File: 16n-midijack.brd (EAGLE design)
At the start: 248.9 x 120.7 mm, 108 parts, among them J1 PJ302M, J10 PJ302M, J11 PJ302M, J12 PJ302M, J13 PJ302M, J14 PJ302M, J15 PJ302M, J16 PJ302M, J2 PJ302M, J3 PJ302M, J4 PJ302M, J5 PJ302M, J6 PJ302M, J7 PJ302M, J8 PJ302M, J9 PJ302M, U1 MCP6004_SMD, U2 MCP6004_SMD, U3 MCP6004_SMD, U4 MCP6004_SMD, U5 MCP6004_SMD, U6 MCP6004_SMD, U7 MCP6004_SMD, U8 MCP6004_SMD

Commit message: Correcting outputs.
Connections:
- removed net N$11: R17.1, U3.8, U3.9
- removed net N$14: R22.1, U4.8, U4.9
- removed net N$17: R27.1, U5.8, U5.9
- removed net N$20: R32.1, U6.8, U6.9
- removed net N$23: R37.1, U7.8, U7.9
- removed net N$256: R12.1, U1.13, U1.14
- removed net N$257: R45.1, U2.13, U2.14
- removed net N$258: R47.1, U3.13, U3.14
- removed net N$259: R46.1, U4.13, U4.14
- removed net N$26: R42.1, U8.8, U8.9
- removed net N$260: R48.1, U5.13, U5.14
- removed net N$261: R49.1, U6.13, U6.14
- removed net N$262: R50.1, U7.13, U7.14
- removed net N$263: R51.1, U8.13, U8.14
- removed net N$5: R52.1, U2.8, U2.9
- removed net N$8: R7.1, U1.8, U1.9
- net A0: now also R7.1, U1.8, U1.9
- net A1: now also R12.1, U1.13, U1.14
- net A10: now also R32.1, U6.8, U6.9
- net A11: now also R49.1, U6.13, U6.14
- net A12: now also R37.1, U7.8, U7.9
- net A13: now also R50.1, U7.13, U7.14
- net A14: now also R42.1, U8.8, U8.9
- net A15: now also R51.1, U8.13, U8.14
- net A2: now also R52.1, U2.8, U2.9
- net A3: now also R45.1, U2.13, U2.14
- net A4: now also R17.1, U3.8, U3.9
- net A5: now also R47.1, U3.13, U3.14
- net A6: now also R22.1, U4.8, U4.9
- net A7: now also R46.1, U4.13, U4.14
- net A8: now also R27.1, U5.8, U5.9
- net A9: now also R48.1, U5.13, U5.14
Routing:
- net N$8: track 140.4 -> 0.00 mm
- net A0: track 32.3 -> 169.5 mm
- net N$5: track 123.3 -> 0.00 mm
- net A2: track 64.1 -> 183.2 mm
- net N$256: track 117.9 -> 0.00 mm
- net N$11: track 116.9 -> 0.00 mm
- net A4: track 91.8 -> 205.8 mm
- net N$263: track 110.8 -> 0.00 mm
- net N$257: track 108.8 -> 0.00 mm
- net N$14: track 107.4 -> 0.00 mm
- net A6: track 120.5 -> 225.1 mm
- net N$17: track 102.5 -> 0.00 mm
- net N$26: track 101.8 -> 0.00 mm, vias 2 -> 0
- net N$258: track 100.3 -> 0.00 mm
- net A14: track 204.6 -> 303.3 mm, vias 2 -> 4
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
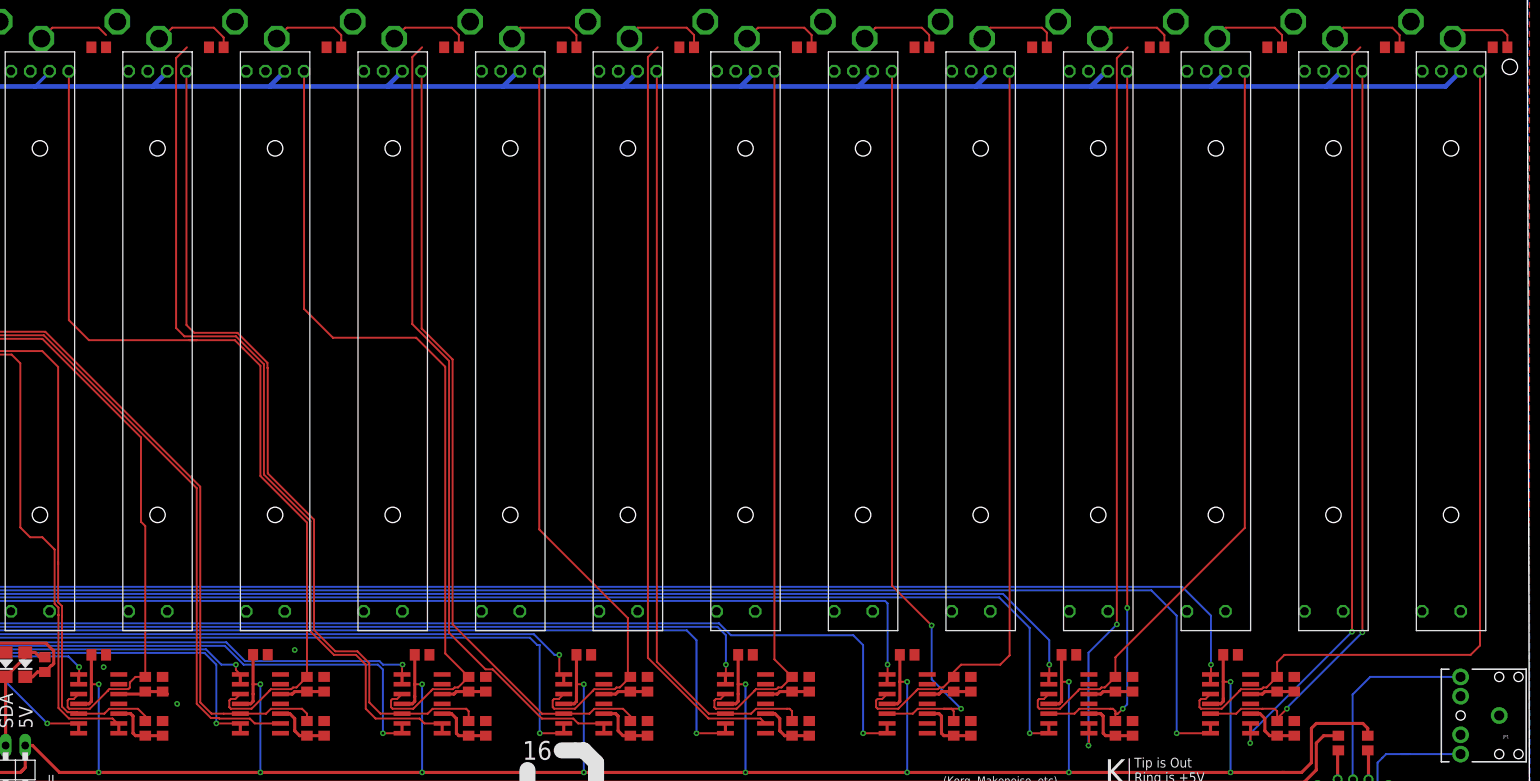
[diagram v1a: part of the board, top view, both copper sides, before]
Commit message: Remove legacy trace names.
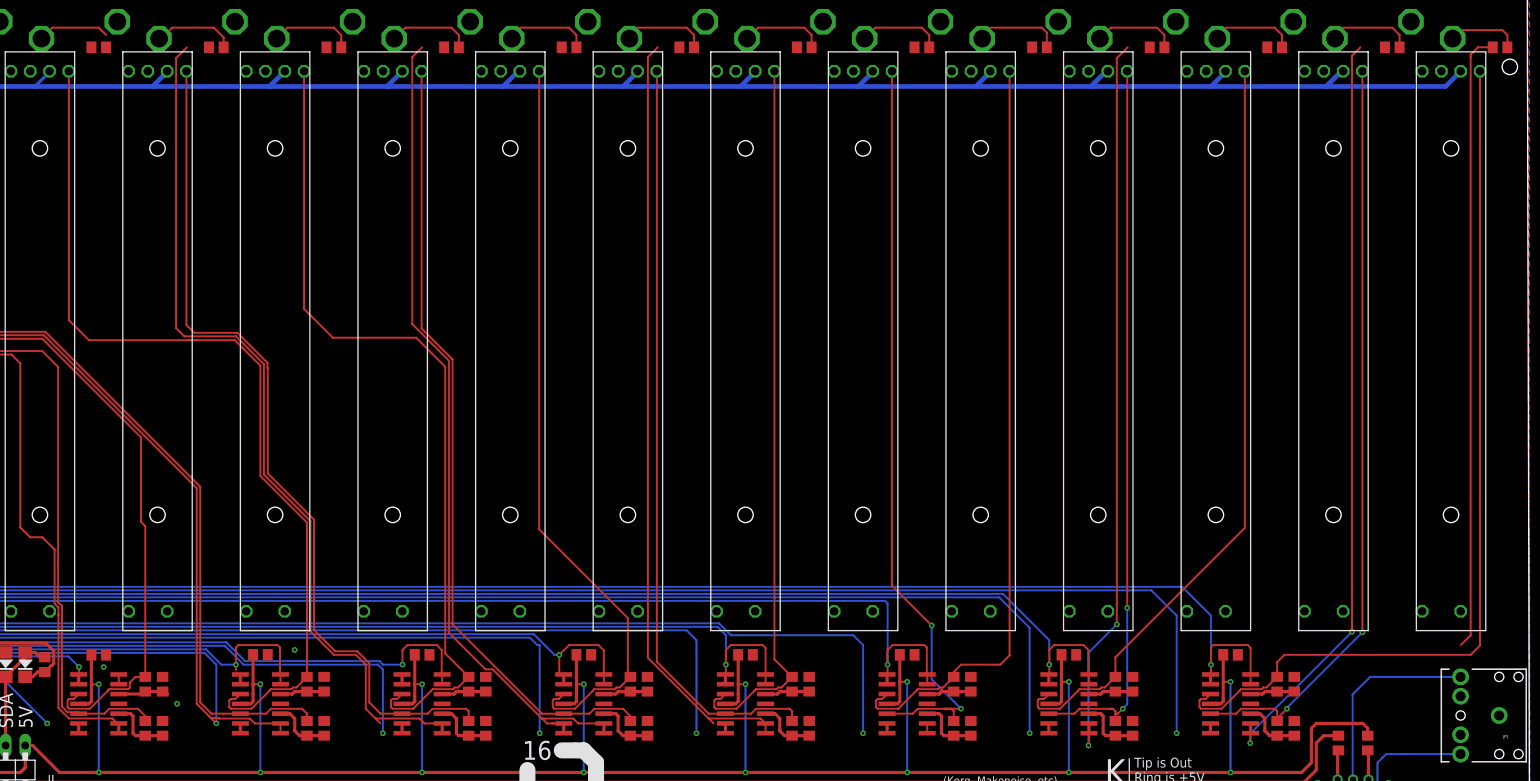
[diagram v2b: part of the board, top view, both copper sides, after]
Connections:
- new net N$300: R7.1, U1.6, U1.7
- new net N$301: R12.1, U1.1, U1.2
- new net N$302: R52.1, U2.6, U2.7
- new net N$303: R45.1, U2.1, U2.2
- new net N$304: R17.1, U3.6, U3.7
- new net N$305: R47.1, U3.1, U3.2
- new net N$306: R22.1, U4.6, U4.7
- new net N$307: R46.1, U4.1, U4.2
- new net N$308: R27.1, U5.6, U5.7
- new net N$309: R48.1, U5.1, U5.2
- new net N$310: R32.1, U6.6, U6.7
- new net N$311: R49.1, U6.1, U6.2
- new net N$312: R37.1, U7.6, U7.7
- new net N$313: R50.1, U7.1, U7.2
- new net N$314: R42.1, U8.6, U8.7
- new net N$315: R51.1, U8.1, U8.2
- net A0: no longer R7.1, U1.6, U1.7
- net A1: no longer R12.1, U1.1, U1.2
- net A10: no longer R32.1, U6.6, U6.7
- net A11: no longer R49.1, U6.1, U6.2
- net A12: no longer R37.1, U7.6, U7.7
- net A13: no longer R50.1, U7.1, U7.2
- net A14: no longer R42.1, U8.6, U8.7
- net A15: no longer R51.1, U8.1, U8.2
- net A2: no longer R52.1, U2.6, U2.7
- net A3: no longer R45.1, U2.1, U2.2
- net A4: no longer R17.1, U3.6, U3.7
- net A5: no longer R47.1, U3.1, U3.2
- net A6: no longer R22.1, U4.6, U4.7
- net A7: no longer R46.1, U4.1, U4.2
- net A8: no longer R27.1, U5.6, U5.7
- net A9: no longer R48.1, U5.1, U5.2
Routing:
- net N$315: track 0.00 -> 81.6 mm
- net A15: track 209.3 -> 220.3 mm
- net A3: track 60.3 -> 71.2 mm
- net A9: track 143.5 -> 154.3 mm
- net A11: track 184.4 -> 195.2 mm
- net A13: track 222.6 -> 233.3 mm
- net A5: track 87.5 -> 97.0 mm
- net A7: track 115.1 -> 124.2 mm
- net A14: track 303.3 -> 297.6 mm
- net A0: track 169.5 -> 164.1 mm
- net A12: track 315.9 -> 312.1 mm
- net A10: track 177.8 -> 174.7 mm
- net A4: track 205.8 -> 202.9 mm
- net A8: track 246.1 -> 243.3 mm
- net A6: track 225.1 -> 222.9 mm
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
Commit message: Fix gate positions.
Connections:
- net A0: now also U1.6, U1.7; no longer U1.8, U1.9
- net A1: now also U1.8, U1.9; no longer U1.13, U1.14
- net A10: now also U6.6, U6.7; no longer U6.8, U6.9
- net A11: now also U6.8, U6.9; no longer U6.13, U6.14
- net A12: now also U7.6, U7.7; no longer U7.8, U7.9
- net A13: now also U7.8, U7.9; no longer U7.13, U7.14
- net A14: now also U8.6, U8.7; no longer U8.8, U8.9
- net A15: now also U8.8, U8.9; no longer U8.13, U8.14
- net A2: now also U2.6, U2.7; no longer U2.8, U2.9
- net A3: now also U2.8, U2.9; no longer U2.13, U2.14
- net A4: now also U3.6, U3.7; no longer U3.8, U3.9
- net A5: now also U3.8, U3.9; no longer U3.13, U3.14
- net A6: now also U4.6, U4.7; no longer U4.8, U4.9
- net A7: now also U4.8, U4.9; no longer U4.13, U4.14
- net A8: now also U5.6, U5.7; no longer U5.8, U5.9
- net A9: now also U5.8, U5.9; no longer U5.13, U5.14
- net N$10: now also U1.10; no longer U1.12
- net N$12: now also U3.5; no longer U3.10
- net N$13: now also U3.10; no longer U3.12
- net N$15: now also U4.5; no longer U4.10
- net N$16: now also U4.10; no longer U4.12
- net N$18: now also U5.5; no longer U5.10
- net N$19: now also U5.10; no longer U5.12
- net N$21: now also U6.5; no longer U6.10
- net N$22: now also U6.10; no longer U6.12
- net N$24: now also U7.5; no longer U7.10
- net N$25: now also U7.10; no longer U7.12
- net N$27: now also U8.5; no longer U8.10
- net N$28: now also U8.10; no longer U8.12
- net N$300: now also U1.1, U1.2; no longer U1.6, U1.7
- net N$301: now also U1.13, U1.14; no longer U1.1, U1.2
- net N$302: now also U2.1, U2.2; no longer U2.6, U2.7
- net N$303: now also U2.13, U2.14; no longer U2.1, U2.2
- net N$304: now also U3.1, U3.2; no longer U3.6, U3.7
- net N$305: now also U3.13, U3.14; no longer U3.1, U3.2
- net N$306: now also U4.1, U4.2; no longer U4.6, U4.7
- net N$307: now also U4.13, U4.14; no longer U4.1, U4.2
- net N$308: now also U5.1, U5.2; no longer U5.6, U5.7
- net N$309: now also U5.13, U5.14; no longer U5.1, U5.2
- net N$310: now also U6.1, U6.2; no longer U6.6, U6.7
- net N$311: now also U6.13, U6.14; no longer U6.1, U6.2
- net N$312: now also U7.1, U7.2; no longer U7.6, U7.7
- net N$313: now also U7.13, U7.14; no longer U7.1, U7.2
- net N$314: now also U8.1, U8.2; no longer U8.6, U8.7
- net N$315: now also U8.13, U8.14; no longer U8.1, U8.2
- net N$6: now also U2.5; no longer U2.10
- net N$7: now also U2.10; no longer U2.12
- net N$9: now also U1.5; no longer U1.10
- net W0: now also U1.3; no longer U1.5
- net W1: now also U1.12; no longer U1.3
- net W10: now also U6.3; no longer U6.5
- net W11: now also U6.12; no longer U6.3
- net W12: now also U7.3; no longer U7.5
- net W13: now also U7.12; no longer U7.3
- net W14: now also U8.3; no longer U8.5
- net W15: now also U8.12; no longer U8.3
- net W2: now also U2.3; no longer U2.5
- net W3: now also U2.12; no longer U2.3
- net W4: now also U3.3; no longer U3.5
- net W5: now also U3.12; no longer U3.3
- net W6: now also U4.3; no longer U4.5
- net W7: now also U4.12; no longer U4.3
- net W8: now also U5.3; no longer U5.5
- net W9: now also U5.12; no longer U5.3
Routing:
- net A12: track 312.1 -> 0.00 mm, vias 3 -> 0
- net A14: track 297.6 -> 0.00 mm, vias 4 -> 0
- net A8: track 243.3 -> 0.00 mm, vias 1 -> 0
- net A6: track 222.9 -> 0.00 mm, vias 1 -> 0
- net A15: track 220.3 -> 0.00 mm, vias 2 -> 0
- net A4: track 202.9 -> 0.00 mm, vias 1 -> 0
- net A11: track 195.2 -> 0.00 mm, vias 1 -> 0
- net A13: track 233.3 -> 48.6 mm, vias 1 -> 0
- net A2: track 181.2 -> 0.00 mm, vias 1 -> 0
- net A10: track 174.7 -> 0.00 mm, vias 1 -> 0
- net A9: track 154.3 -> 0.00 mm, vias 1 -> 0
- net W0: track 137.3 -> 0.00 mm
- net A0: track 164.1 -> 32.3 mm
- net W1: track 124.3 -> 0.00 mm
- net A7: track 124.2 -> 0.00 mm, vias 1 -> 0
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
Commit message: WIP: rerouting.
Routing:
- net W0: track 0.00 -> 140.0 mm
- net W2: track 0.00 -> 130.0 mm
- net N$300: track 1.27 -> 128.9 mm
- net W1: track 0.00 -> 124.4 mm
- net N$302: track 0.00 -> 119.1 mm
- net N$301: track 1.27 -> 120.3 mm
- net W3: track 0.00 -> 113.7 mm
- net N$303: track 0.00 -> 109.2 mm
- net A3: track 0.00 -> 69.8 mm, vias 0 -> 1
- net A2: track 0.00 -> 63.5 mm, vias 0 -> 1
- net A1: track 1.27 -> 40.9 mm, vias 0 -> 1
- net A12: track 0.00 -> 33.9 mm
- net A5: track 0.00 -> 30.2 mm
- net A7: track 0.00 -> 26.1 mm
- net A8: track 0.00 -> 24.6 mm
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
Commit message: Completed reroute. Blimey.
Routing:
- net A15: track 0.00 -> 246.7 mm, vias 0 -> 2
- net A14: track 0.00 -> 244.1 mm, vias 0 -> 2
- net A12: track 33.9 -> 221.1 mm, vias 0 -> 1
- net A13: track 49.6 -> 236.3 mm, vias 0 -> 1
- net A11: track 24.4 -> 189.2 mm, vias 0 -> 1
- net A10: track 18.2 -> 177.1 mm, vias 0 -> 1
- net A9: track 12.1 -> 152.3 mm, vias 0 -> 1
- net A8: track 24.6 -> 146.8 mm, vias 0 -> 1
- net W15: track 0.00 -> 115.9 mm
- net W14: track 0.00 -> 113.5 mm
- net W6: track 0.00 -> 111.0 mm
- net N$315: track 1.27 -> 110.6 mm
- net N$304: track 1.27 -> 109.0 mm
- net W4: track 15.1 -> 122.3 mm
- net W12: track 0.00 -> 106.4 mm
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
